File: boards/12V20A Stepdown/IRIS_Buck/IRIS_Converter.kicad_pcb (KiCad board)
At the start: 2 copper layers, 26 parts, among them J1 TB005-762-02BE, J2 TB005-762-02BE, Q1 CSD17571Q2, Q2 CSD16340Q3, U1 LM25145RGYR

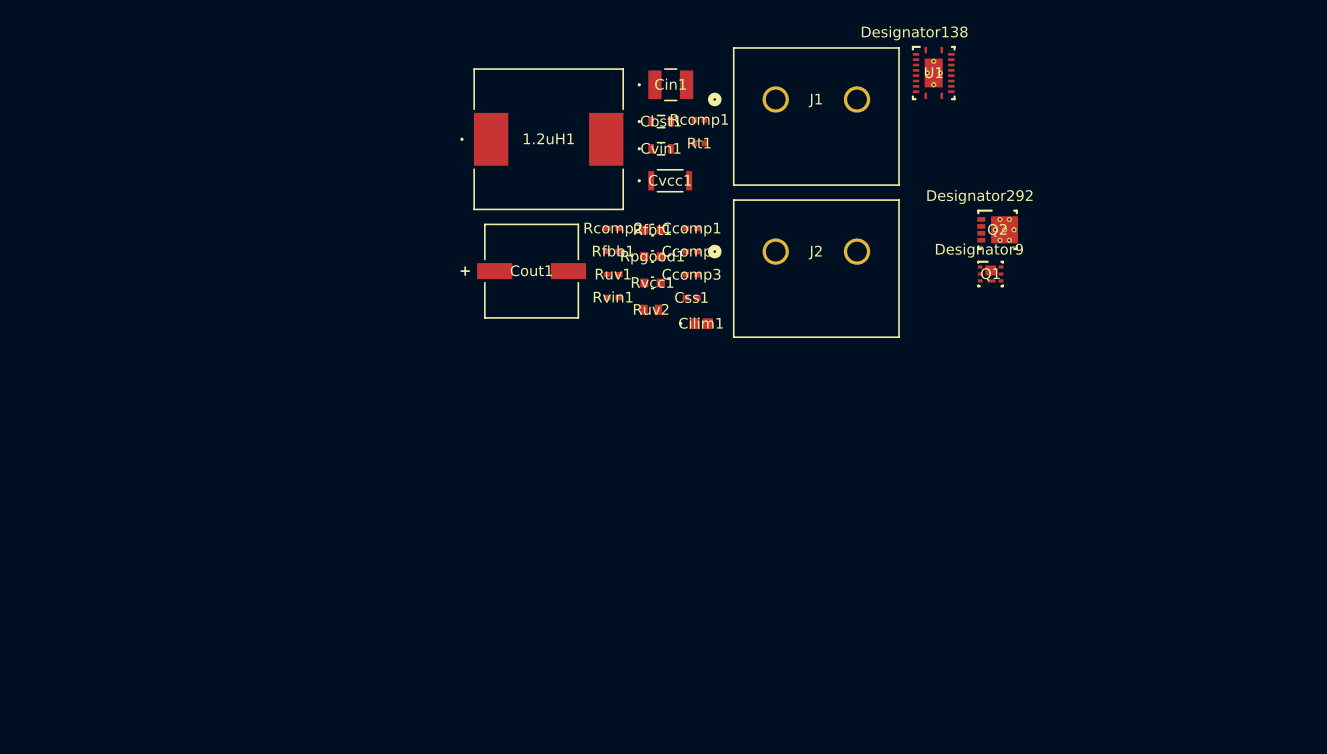
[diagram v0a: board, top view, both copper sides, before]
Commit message: Finished front and back layout, will check via stitching later
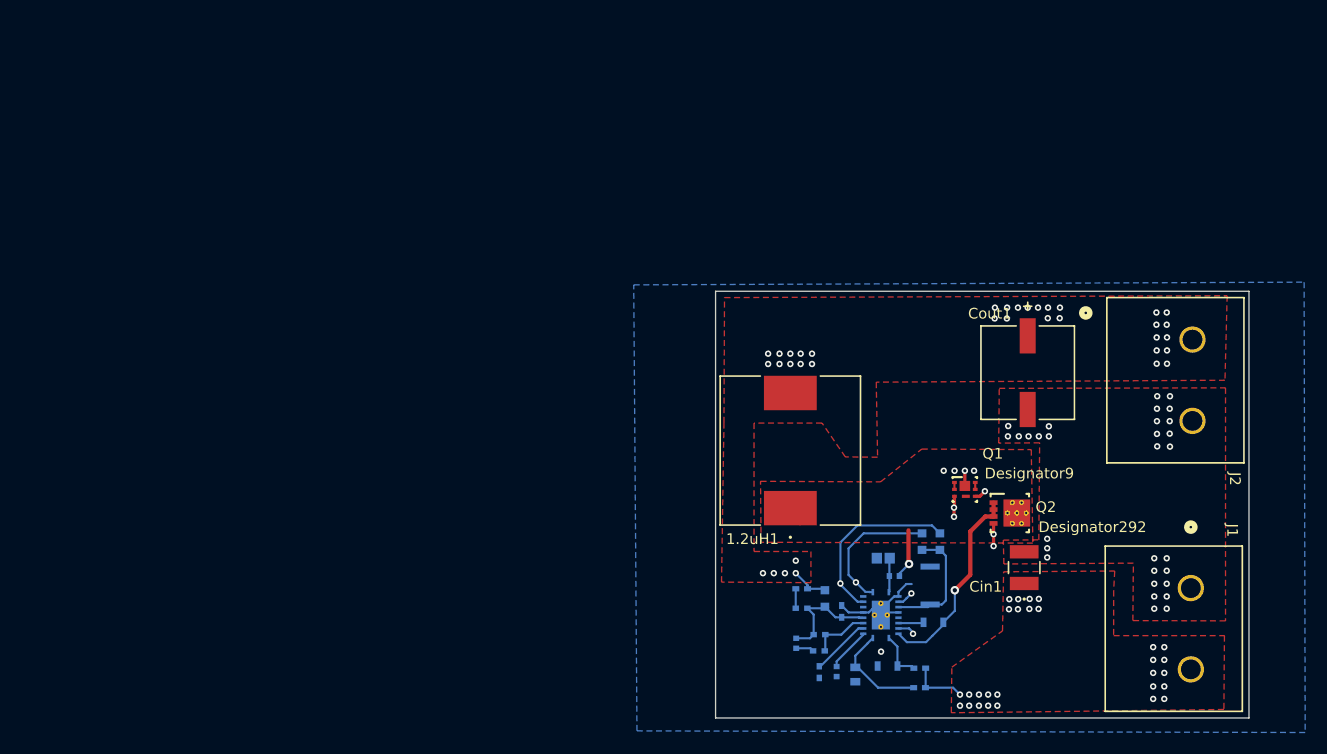
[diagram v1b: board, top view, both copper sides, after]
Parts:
- added Rilim1: 1.1kOhm, 20A_Library:RES_CRCW_0402, B.Cu at (149.5, 88.7)
- Cbst1, Ccomp1, Ccomp2, Ccomp3, Cilim1, Css1, Cvcc1, Cvin1, Rcomp1, Rcomp2, Rfbb1, Rfbt1, Rpgood1, Rt1, Ruv1, Ruv2, Rvcc1, Rvin1, U1: moved to B.Cu
- moved J1 60.1 mm to (177.3, 89.8), turned to -90 degrees
- moved Cin1 56.1 mm to (161.7, 87.9), turned to 90 degrees
- moved Cbst1 53.4 mm to (153.2, 93.0)
- moved Cvin1 52.9 mm to (148.9, 97.1)
- moved Rt1 51.1 mm to (144.1, 97.6), turned to -90 degrees
- moved U1 51.1 mm to (148.2, 92.3)
- moved Rcomp1 49.9 mm to (140.3, 95.0), turned to 90 degrees
- moved Ruv1 48.2 mm to (151.9, 99.1), turned to 180 degrees
- moved Cout1 47.5 mm to (162.0, 69.6), turned to -90 degrees
- moved Cvcc1 45.1 mm to (152.9, 89.5), turned to 90 degrees
- moved Rvin1 45.1 mm to (151.9, 97.3), turned to 180 degrees
- moved Ccomp1 41.4 mm to (142.4, 95.7), turned to 180 degrees
- moved Rfbb1 40.0 mm to (144.6, 92.0), turned to 90 degrees
- moved J2 39.9 mm to (177.4, 66.5), turned to -90 degrees
- moved Ruv2 39.2 mm to (145.8, 97.9), turned to -90 degrees
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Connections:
- net Net-(Cin1-Pad1) renamed /Vin
- net Net-(U1-EN/UVLO) renamed /EN/UVLO
- net Net-(U1-SS/TRK) renamed /SS/TRK
- net Net-(U1-SW) renamed /SW
- net Net-(U1-SYNCIN) renamed /SYNCin
- 1.2uH1 pad 2: Net-(1.2uH1-Pad2) -> /Vout
- Cout1 pad 1: Net-(1.2uH1-Pad2) -> /Vout
- J2 pad 1: GND -> /Vout
- J2 pad 2: Net-(1.2uH1-Pad2) -> GND
- Q2 pad 5: (no net) -> GND
- Q2 pad 6: (no net) -> GND
- Q2 pad 7: (no net) -> GND
- Q2 pad 8: (no net) -> GND
- Q2 pad 9: (no net) -> GND
- Q2 pad V: (no net) -> GND
- Rcomp2 pad 1: Net-(1.2uH1-Pad2) -> /Vout
- Rfbt1 pad 1: Net-(1.2uH1-Pad2) -> /Vout
- U1 pad V: (no net) -> GND
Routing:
- net /SW: track 0.00 -> 27.2 mm, vias 0 -> 2
- net /SYNCin: track 0.00 -> 17.1 mm, vias 0 -> 1
- net Net-(U1-HO): track 0.00 -> 16.9 mm, vias 0 -> 3
- net GND: track 0.00 -> 13.4 mm, vias 0 -> 36
- net Net-(U1-PGOOD): track 0.00 -> 12.9 mm, vias 0 -> 1
- net Net-(U1-LO): track 0.00 -> 12.3 mm, vias 0 -> 3
- net Net-(U1-VCC): track 0.00 -> 12.1 mm
- net Net-(U1-FB): track 0.00 -> 10.4 mm
- net /EN/UVLO: track 0.00 -> 9.69 mm
- net /SS/TRK: track 0.00 -> 5.60 mm
- net Net-(U1-COMP): track 0.00 -> 5.55 mm
- net /Vin: track 0.00 -> 5.40 mm, vias 0 -> 28
- net Net-(U1-VIN): track 0.00 -> 4.58 mm
- net Net-(U1-RT): track 0.00 -> 4.12 mm
- net /Vout: track 0.00 -> 3.73 mm, vias 0 -> 36
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- added copper zone on F.Cu, net /SW
- added copper zone on F.Cu, net /Vin
- added copper zone on F.Cu, net /Vout
- added copper zone on B.Cu, net GND
- added copper zone on F.Cu, net GND
- added copper zone on In1.Cu, net GND
- added copper zone on In2.Cu, net GND
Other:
- board outline added: 50 x 40 mm
- copper layers 2 -> 4

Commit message: Added via stiching for gnd plane
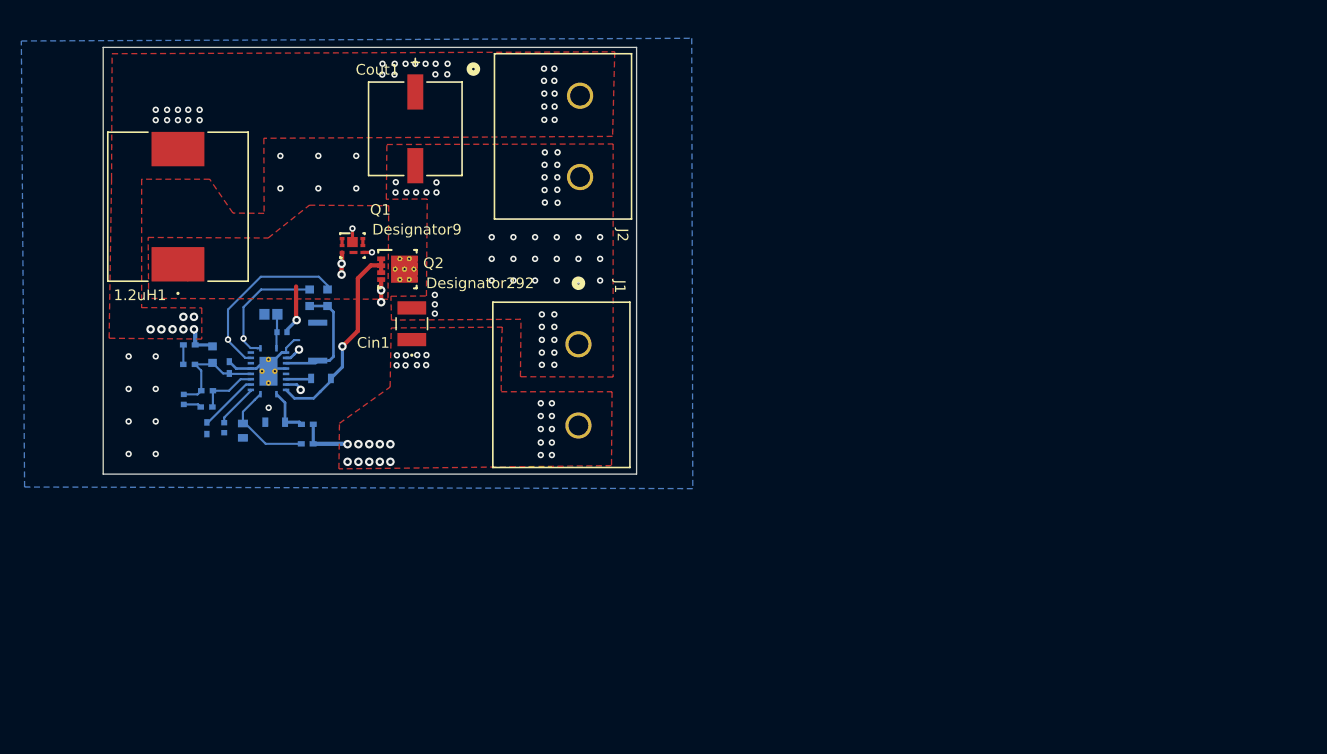
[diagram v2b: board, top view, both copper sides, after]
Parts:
- moved Cout1 61.8 mm to (104.6, 46.7)
- moved Css1 61.8 mm to (85.1, 74.8)
- moved Cvin1 61.8 mm to (91.5, 74.2)
- moved Q2 61.8 mm to (102.9, 59.9)
- moved Rfbt1 61.8 mm to (85.6, 67.9)
- moved Rpgood1 61.8 mm to (94.7, 62.6)
- moved Rvcc1 61.8 mm to (96.4, 62.6)
- moved 1.2uH1 61.8 mm to (82.3, 54.0)
- moved Cbst1 61.8 mm to (95.8, 70.1)
- moved Ccomp2 61.8 mm to (85.1, 71.3)
- moved Ccomp3 61.8 mm to (83.4, 68.8)
- moved Cilim1 61.8 mm to (91.1, 64.1)
- moved Cin1 61.8 mm to (104.3, 65.0)
- moved Cvcc1 61.8 mm to (95.4, 66.7)
- moved J1 61.8 mm to (119.9, 66.9)
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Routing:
- net Net-(U1-PGOOD): track 12.9 -> 11.9 mm
- net /SW: track 27.2 -> 28.0 mm
- net Net-(U1-LO): track 12.3 -> 12.9 mm
- net /Vout: track 3.73 -> 3.32 mm, vias 36 -> 38
- net GND: track 13.4 -> 13.0 mm, vias 36 -> 65
